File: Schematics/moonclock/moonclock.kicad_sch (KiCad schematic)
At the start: 32 parts, among them J1 Conn_01x06, J2 Conn_01x04, J3 Screw_Terminal_01x04, J4 Screw_Terminal_01x04, J5 Screw_Terminal_01x04, J6 Conn_01x04, J7 Conn_01x05, U1 RP2040-Zero, U2 MCP6002-xSN, U3 MCP47FVB22-E/ST, U4 MCP7940N-xSN, Y1 ECS-.327-6-17X-C-TR

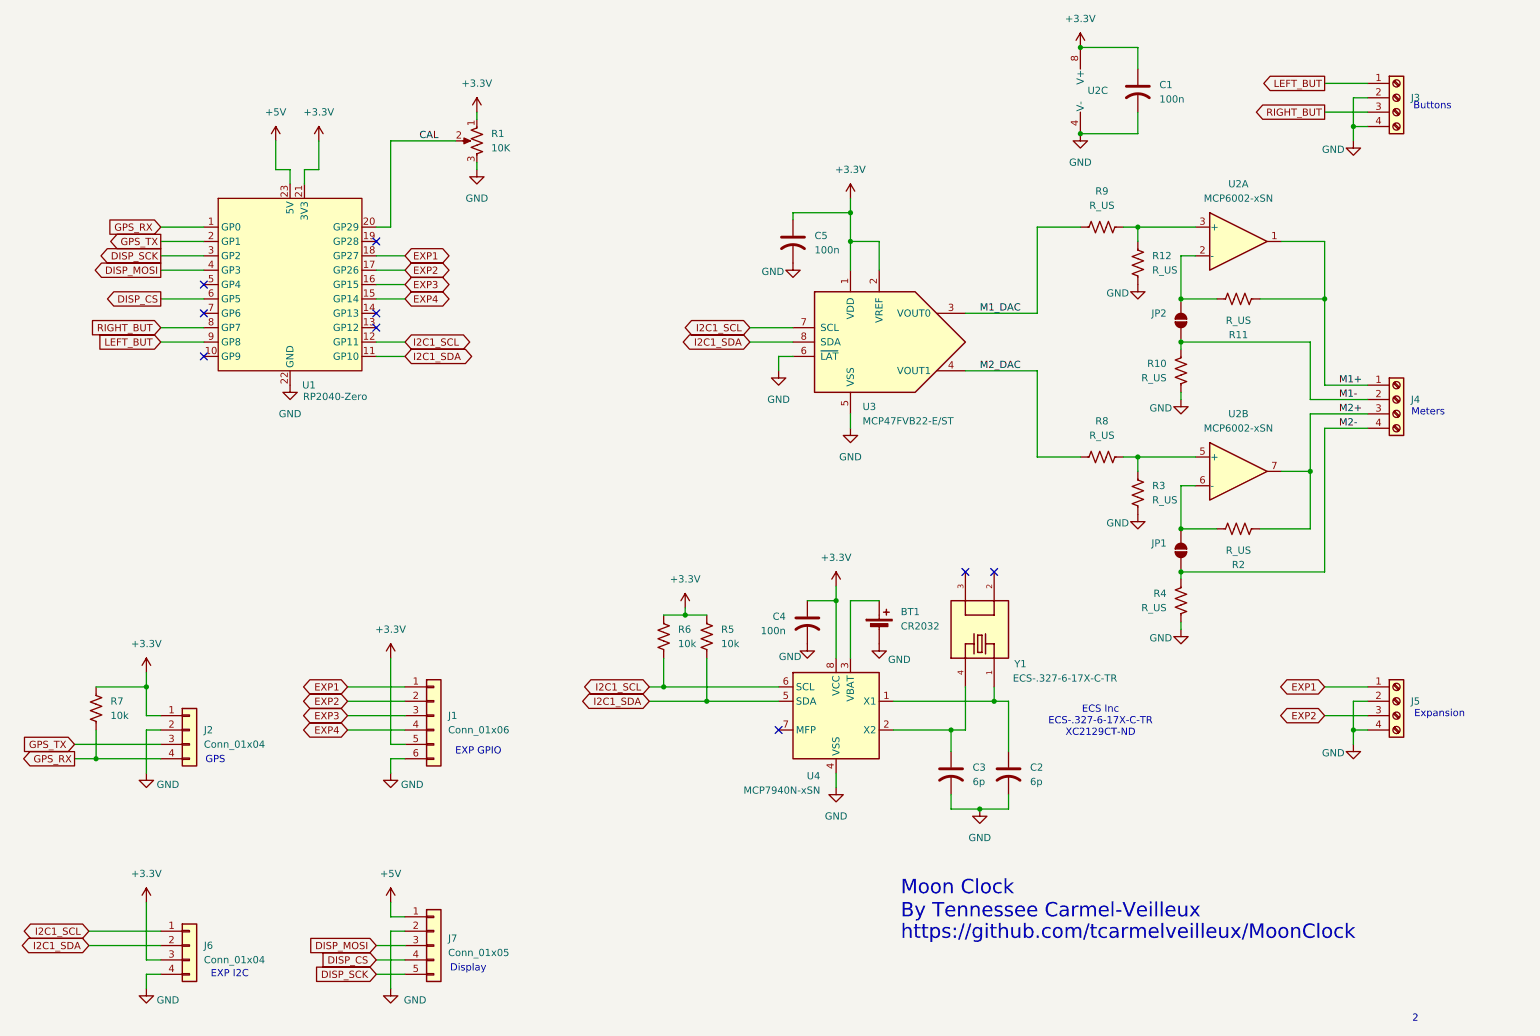
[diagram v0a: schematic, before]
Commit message: Schematic cosmetic improvements and PDF plot
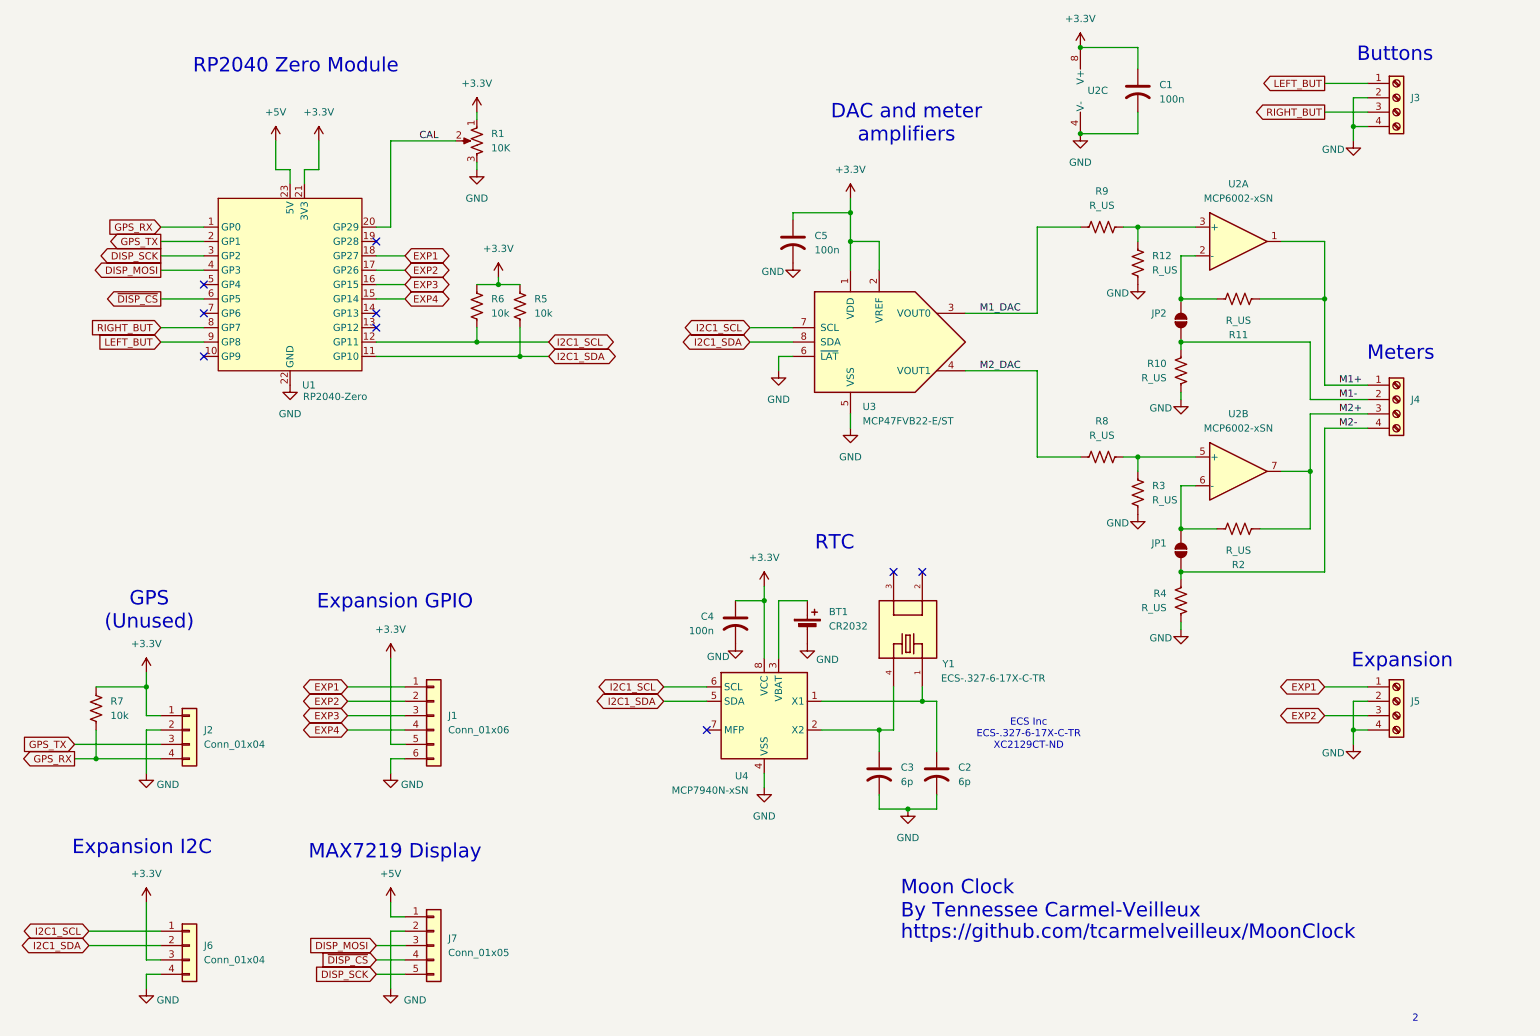
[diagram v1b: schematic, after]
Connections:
- net DISP_CS renamed ~{DISP_CS}
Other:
- note added: "DAC and meter amplifiers"
- note added: "Expansion GPIO"
- note added: "Expansion I2C"
- note added: "GPS (Unused)"
- note added: "MAX7219 Display"
- note added: "RP2040 Zero Module"
- note added: "RTC"
- note removed: "Display"
- note removed: "EXP GPIO"
- note removed: "EXP I2C"
- note removed: "GPS"
- moved on the sheet: BT1, C2, C3, C4, R5, R6, U4, Y1
